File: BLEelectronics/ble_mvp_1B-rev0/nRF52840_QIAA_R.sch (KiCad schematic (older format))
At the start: 40 parts, among them J3 Conn_02x05_Odd_Even, SW1 NO, SW2 SW_MEC_5G, U5 nRF52840, X1 32MHz, X2 32.768KHZ

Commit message: renamed files in mvp1a-rev0 folder, added schematic and gerber pdfs
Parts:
- removed C19: N.C., Capacitor_SMD:C_0201_0603Metric, symbol Device:C
- C10, C11, C12, C13, C14, C15, C17, C18, C20, C21, C22, C23, C24, C25, C26, C27, C28, C29, D5, J3, L1, L2, L3, L4, U5: DPN (none) -> -; LCSCPN (none) -> -; MFR (none) -> -; MPN (none) -> -; SIM (none) -> -; SPN (none) -> -; SPR (none) -> -
- C16, C31: value 100nF -> 0.01uF; DPN (none) -> -; LCSCPN (none) -> -; MFR (none) -> -; MPN (none) -> -; SIM (none) -> -; SPN (none) -> -; SPR (none) -> -
- C30: value 100nF -> 0.1uF; DPN (none) -> -; LCSCPN (none) -> -; MFR (none) -> -; MPN (none) -> -; SIM (none) -> -; SPN (none) -> -; SPR (none) -> -
- D4, SW1, SW2, X1, X2: LCSCPN (none) -> -; SIM (none) -> -; SPN (none) -> -; SPR (none) -> -
- R10: DPN (none) -> YAG2283CT-ND; LCSCPN (none) -> -; MFR (none) -> Yageo; MPN (none) -> RC0201FR-07390RL; SIM (none) -> -; SPN (none) -> -; SPR (none) -> -
- R11: DPN (none) -> 311-0.0NCT-ND; LCSCPN (none) -> -; MFR (none) -> Yageo; MPN (none) -> RC0201JR-070RL; SIM (none) -> -; SPN (none) -> -; SPR (none) -> -
- R12: DPN 311-4.70KHRCT-ND -> YAG3413CT-ND; MPN RC0603FR-074K7L -> AC0201FR-0710KL
- R7: DPN (none) -> P123276CT-ND; LCSCPN (none) -> -; MFR (none) -> Panasonic Electronic Components; MPN (none) -> ERJ-1GNJ221C; SIM (none) -> -; SPN (none) -> -; SPR (none) -> -
- R8: value 1k2 -> 1K2; DPN (none) -> YAG5168CT-ND; LCSCPN (none) -> -; MFR (none) -> Yageo; MPN (none) -> AC0201FR-071K2L; SIM (none) -> -; SPN (none) -> -; SPR (none) -> -
- R9: value 2k2 -> 2K2; DPN (none) -> YAG2572CT-ND; LCSCPN (none) -> -; MFR (none) -> Yageo; MPN (none) -> RC0201FR-072K2L; SIM (none) -> -; SPN (none) -> -; SPR (none) -> -
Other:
- note added: "Removed \nNC cap\nE24-D23"

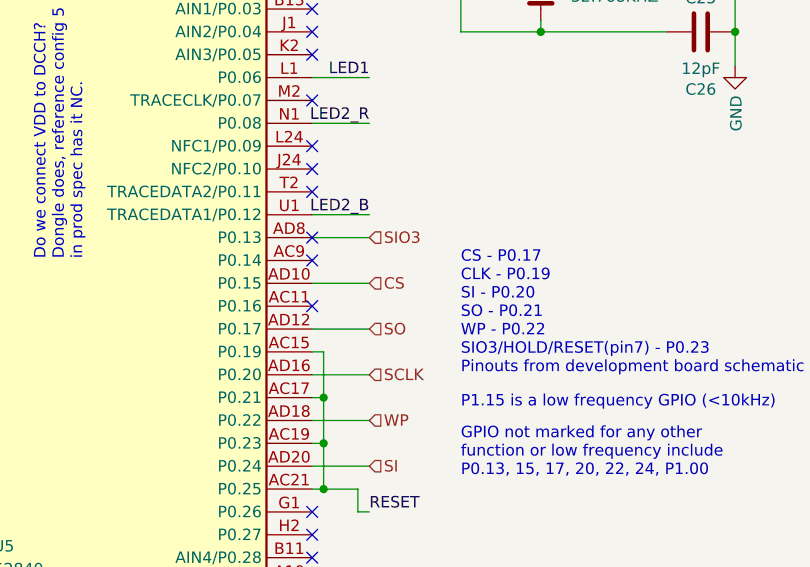
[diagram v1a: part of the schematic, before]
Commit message: correct CS to CS# in schematic and pdfs for all mvps
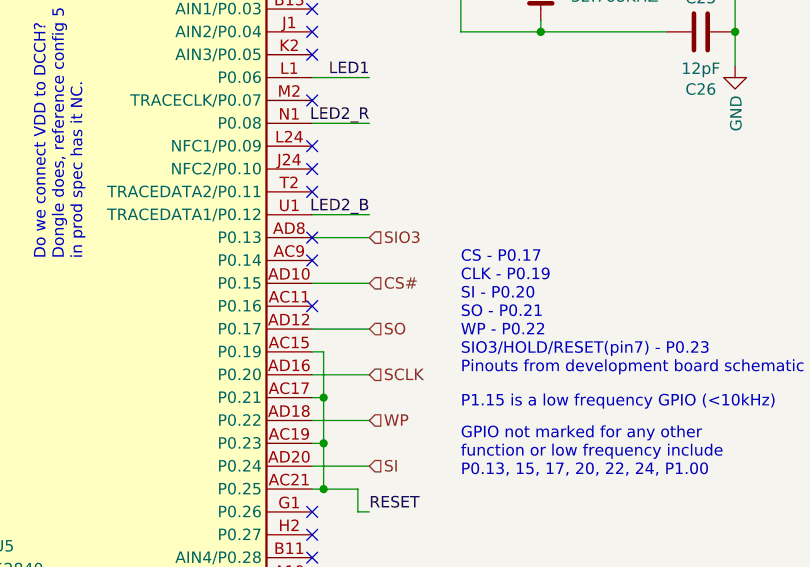
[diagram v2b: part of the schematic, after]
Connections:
- net CS renamed CS#
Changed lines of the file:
@@
 SCL
 Text HLabel 6000 3900 2    50   Input ~ 0
-CS
+CS#
 Text HLabel 6000 4300 2    50   Input ~ 0
 SCLK

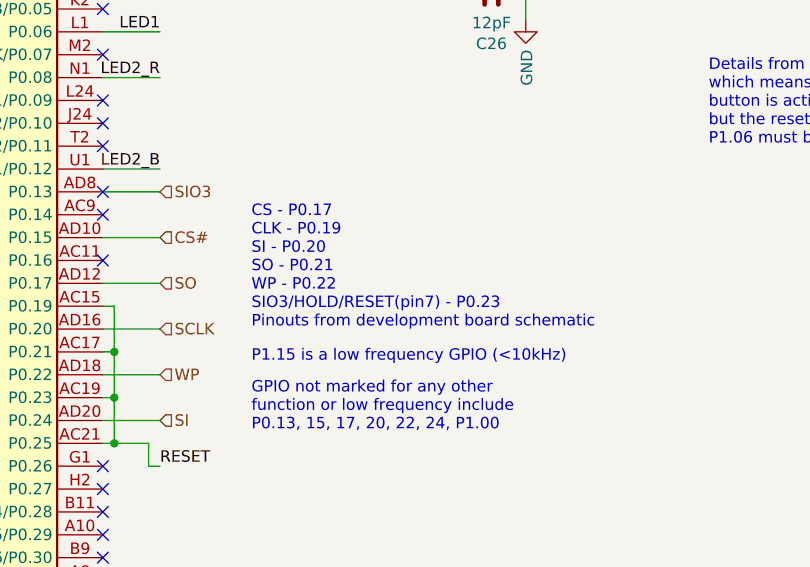
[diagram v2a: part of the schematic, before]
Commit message: Additional changes to schematic labelling.
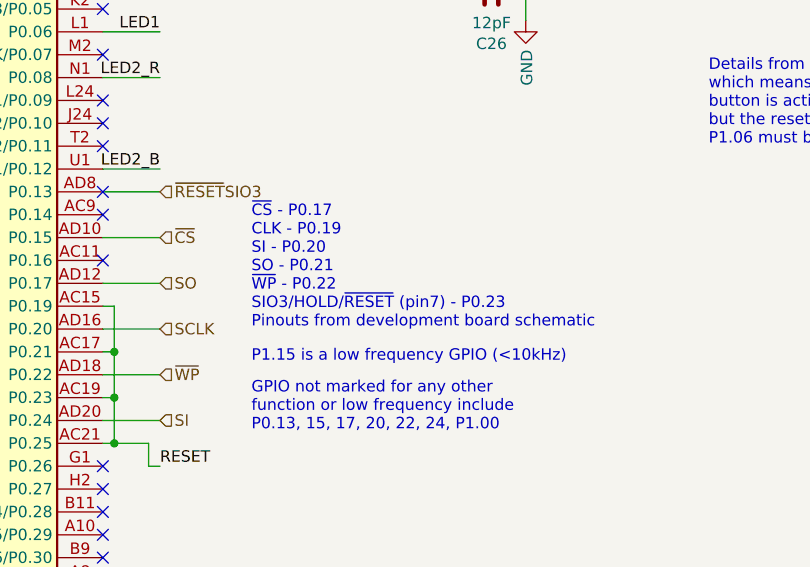
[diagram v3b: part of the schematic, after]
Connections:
- net CS# renamed ~CS
- net SIO3 renamed ~RESET~SIO3
- net WP renamed ~WP
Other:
- note added: "~CS~ - P0.17\nCLK - P0.19\nSI - P0.20\nSO - P0.21\n~WP~ - P0.22\nSIO3/HOLD/~RESET~ (pin7) - P0.23\nPinouts from development board schematic\n"
- note removed: "CS - P0.17\nCLK - P0.19\nSI - P0.20\nSO - P0.21\nWP - P0.22\nSIO3/HOLD/RESET(pin7) - P0.23\nPinouts from development board schematic\n"
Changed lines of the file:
@@
 GPIO not marked for any other \nfunction or low frequency include \nP0.13, 15, 17, 20, 22, 24, P1.00
 Text Notes 6400 4300 0    50   ~ 0
-CS - P0.17\nCLK - P0.19\nSI - P0.20\nSO - P0.21\nWP - P0.22\nSIO3/HOLD/RESET(pin7) - P0.23\nPinouts from development board schematic\n
+~CS~ - P0.17\nCLK - P0.19\nSI - P0.20\nSO - P0.21\n~WP~ - P0.22\nSIO3/HOLD/~RESET~ (pin7) - P0.23\nPinouts from development board schematic\n
 Text Label 6000 3600 2    50   ~ 0
 LED2_B
@@
 SCL
 Text HLabel 6000 3900 2    50   Input ~ 0
-CS#
+~CS
 Text HLabel 6000 4300 2    50   Input ~ 0
 SCLK
@@
 SO
 Text HLabel 6000 4500 2    50   Input ~ 0
-WP
+~WP
 Text HLabel 6000 3700 2    50   Input ~ 0
-SIO3
+~RESET~SIO3
 Text HLabel 6000 7100 2    50   Input ~ 0
 SDA

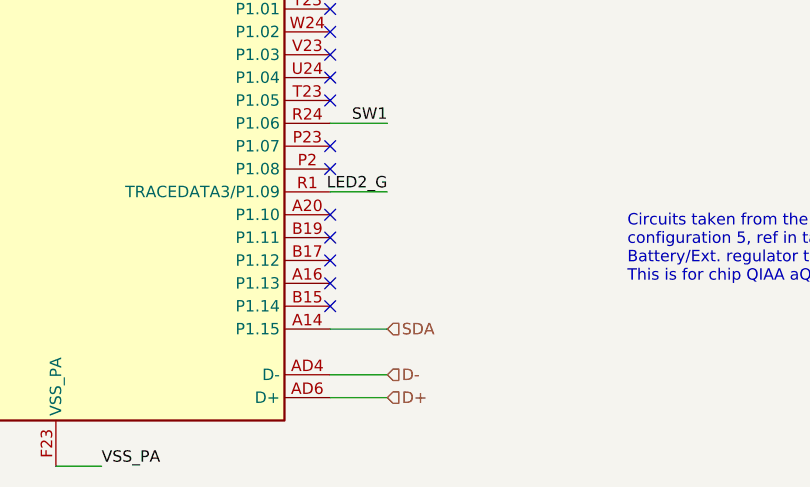
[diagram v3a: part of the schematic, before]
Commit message: increased track widths on long traces on mvp1b-rev0
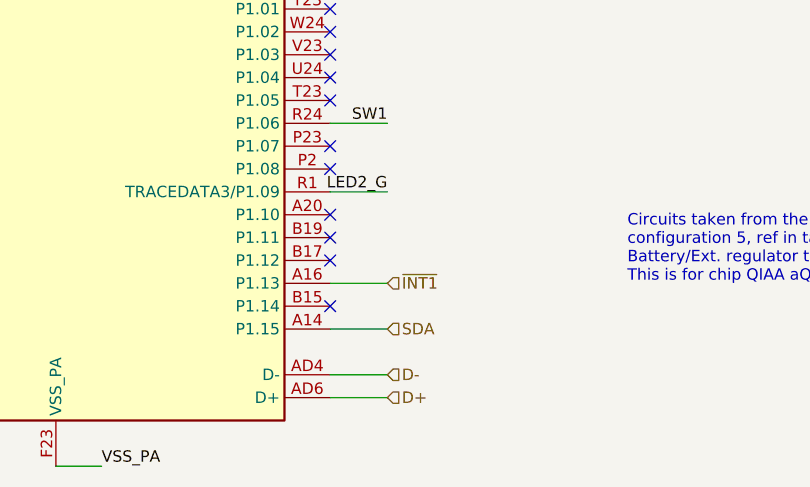
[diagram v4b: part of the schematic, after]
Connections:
- net ~INT1~: now reaches U5.A16 (P1.13)
- no-connect marks 33 -> 32
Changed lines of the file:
@@
 NoConn ~ 5750 6700
 NoConn ~ 5750 6800
-NoConn ~ 5750 6900
 NoConn ~ 5750 7000
 NoConn ~ 5750 3700
@@
 NoConn ~ 10350 5750
 NoConn ~ 3150 6900
+Wire Wire Line
+	6000 6900 5750 6900
+Text HLabel 6000 6900 2    50   Input ~ 0
+~INT1~
 $EndSCHEMATC
